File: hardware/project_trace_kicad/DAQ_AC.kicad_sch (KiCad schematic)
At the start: 55 parts, among them U301 THS4131IDR, U302 MCP6499T, U303 ADS1602, U304 LM4040DBZ-4.1

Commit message: Work on Layout
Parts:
- C303, C304: now not fitted
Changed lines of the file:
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@@
 		(on_board yes)
 		(in_pos_files yes)
-		(dnp no)
+		(dnp yes)
 		(property "Reference" "C303"
 			(at 35.179 136.4572 0)
@@
 		(on_board yes)
 		(in_pos_files yes)
-		(dnp no)
+		(dnp yes)
 		(property "Reference" "C304"
 			(at 47.879 136.4572 0)

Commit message: Rework started
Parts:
- removed C303, C304: 47u, Capacitor_THT:CP_Radial_D6.3mm_P2.50mm, symbol Device:C_Polarized

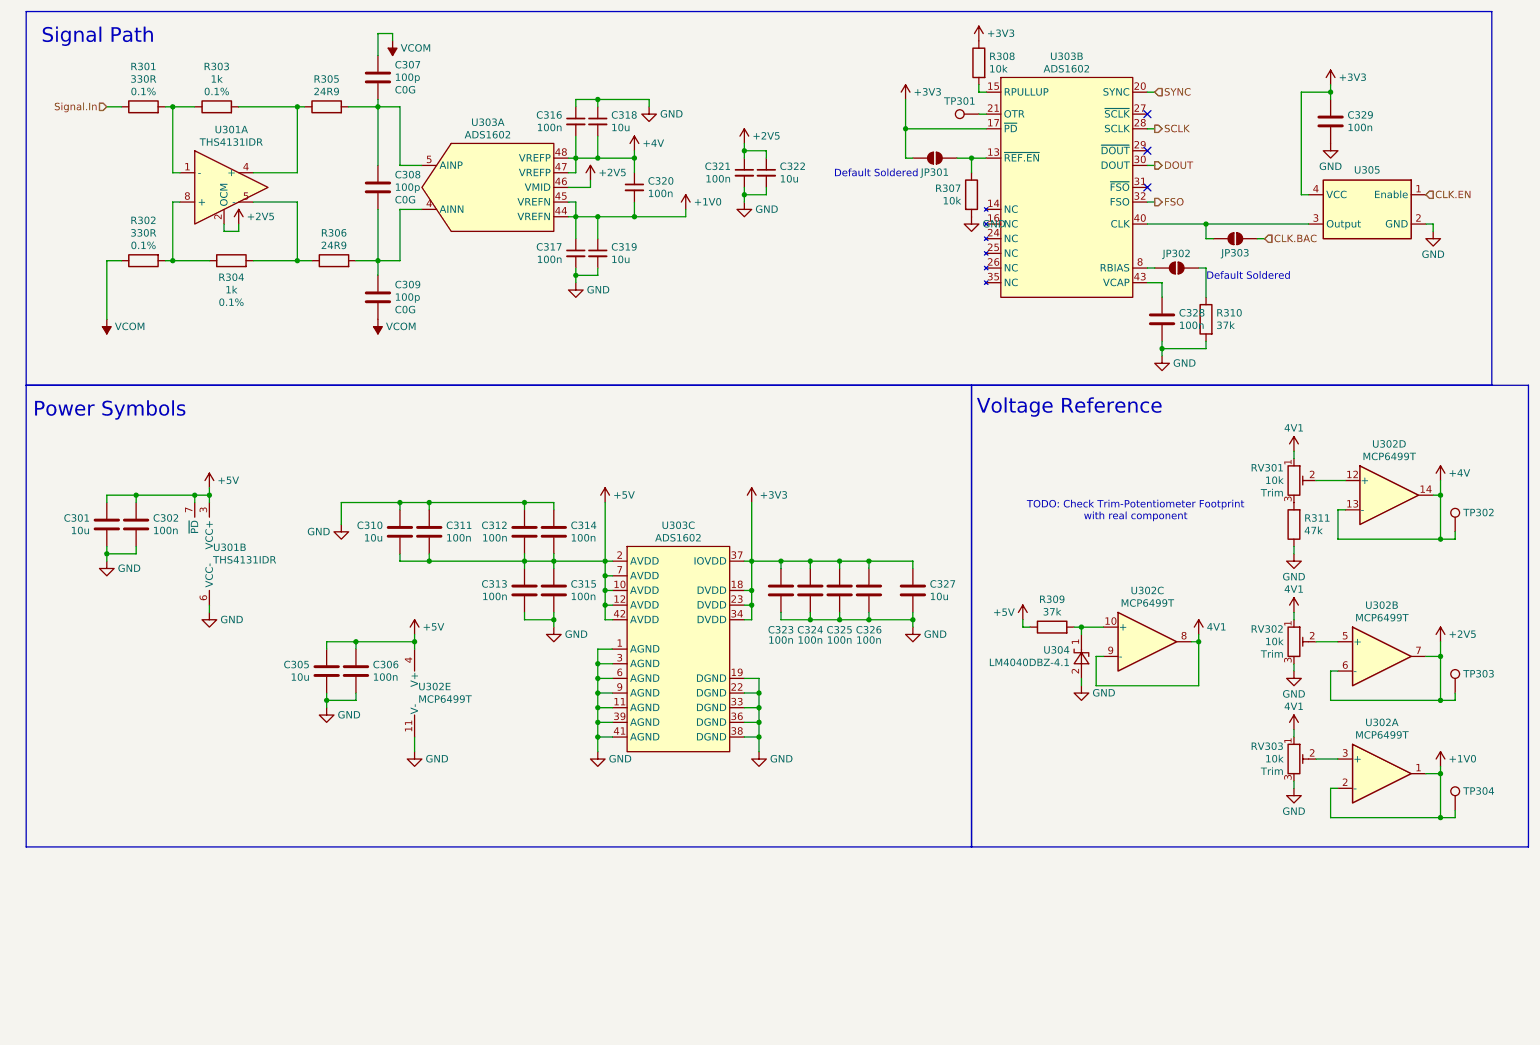
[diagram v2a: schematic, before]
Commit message: Fix inconsistency with ADC datasheet, fix DRC Errors
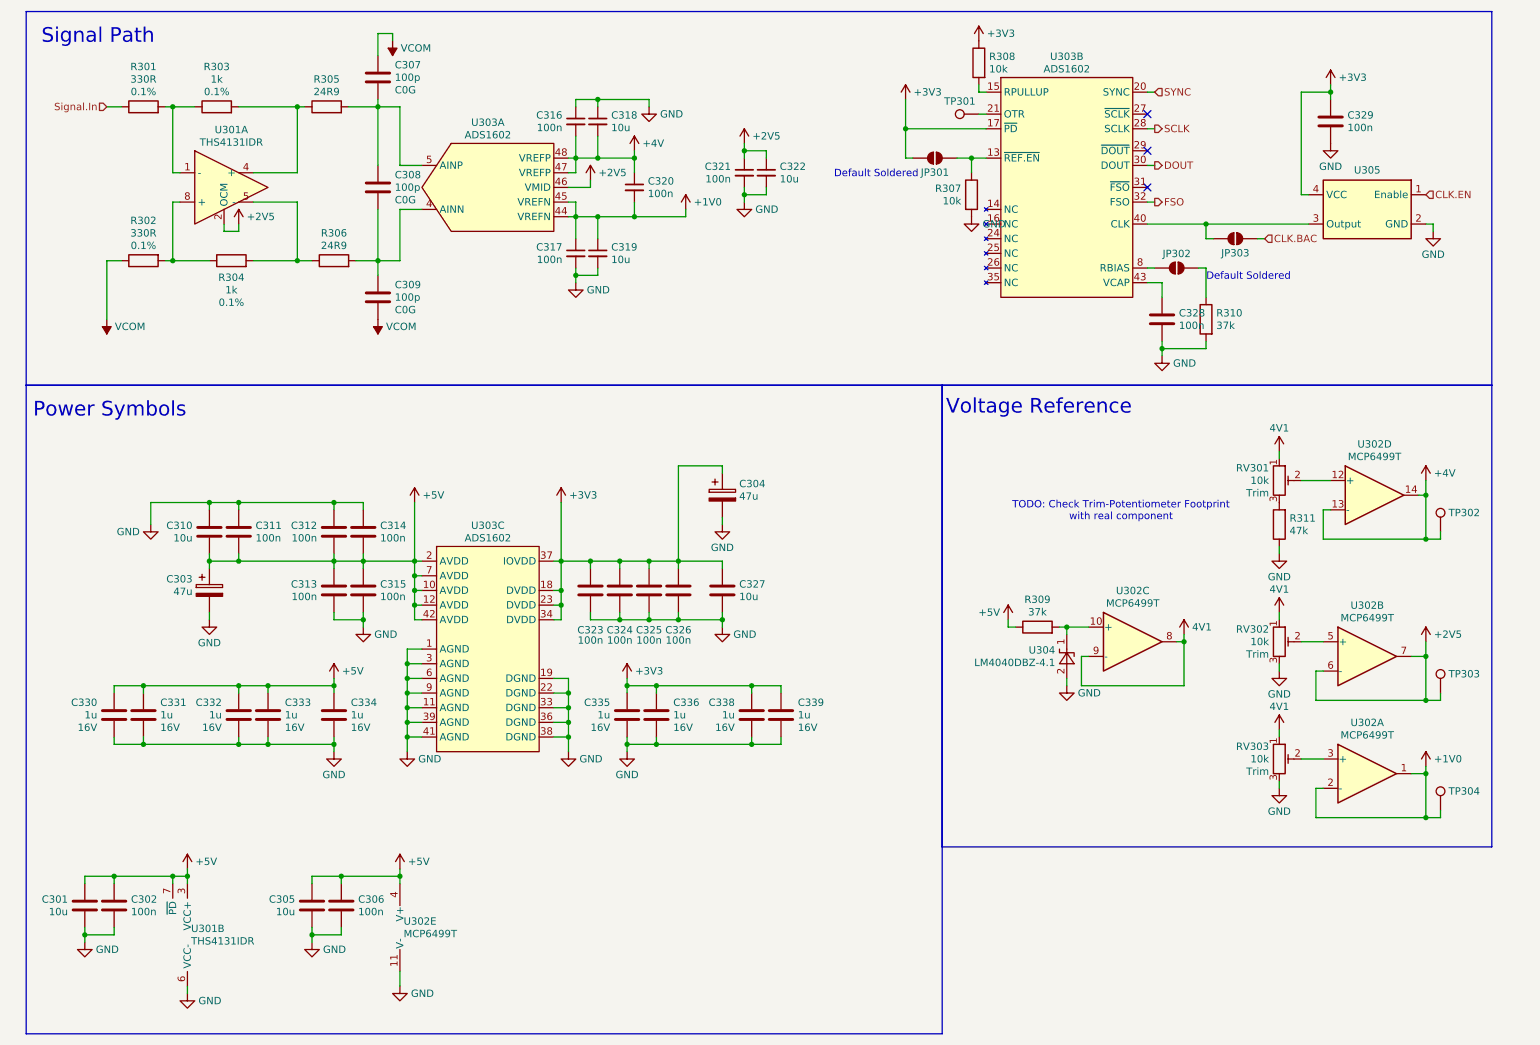
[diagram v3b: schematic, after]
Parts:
- added C303, C304: 47u, Capacitor_THT:CP_Radial_D6.3mm_P2.50mm, symbol Device:C_Polarized
- added C330, C331, C332, C333, C334, C335, C336, C338, C339: 1u, Capacitor_SMD:C_0603_1608Metric_Pad1.08x0.95mm_HandSolder, symbol Device:C
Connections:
- net +3V3: now also C304.1, C335.2, C336.2, C338.2, C339.2
- net +5V: now also C303.1, C330.2, C331.2, C332.2, C333.2, C334.2
- net GND: now also C303.2, C304.2, C330.1, C331.1, C332.1, C333.1, C334.1, C335.1, C336.1, C338.1, C339.1
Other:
- moved on the sheet: C301, C302, C305, C306, C310, C311, C312, C313, C314, C315, C323, C324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

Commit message: Improvements to Power layout and Silkscreen
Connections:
- net ADC.CLK_IN: now reaches JP303.2 (B), U303.40 (CLK), U305.3 (Output)

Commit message: Pre Diffamp
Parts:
- added C337: 100n, Capacitor_SMD:C_0603_1608Metric_Pad1.08x0.95mm_HandSolder, symbol Device:C_Small
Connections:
- net +2V5: now also C337.1
- net GND: now also C337.2

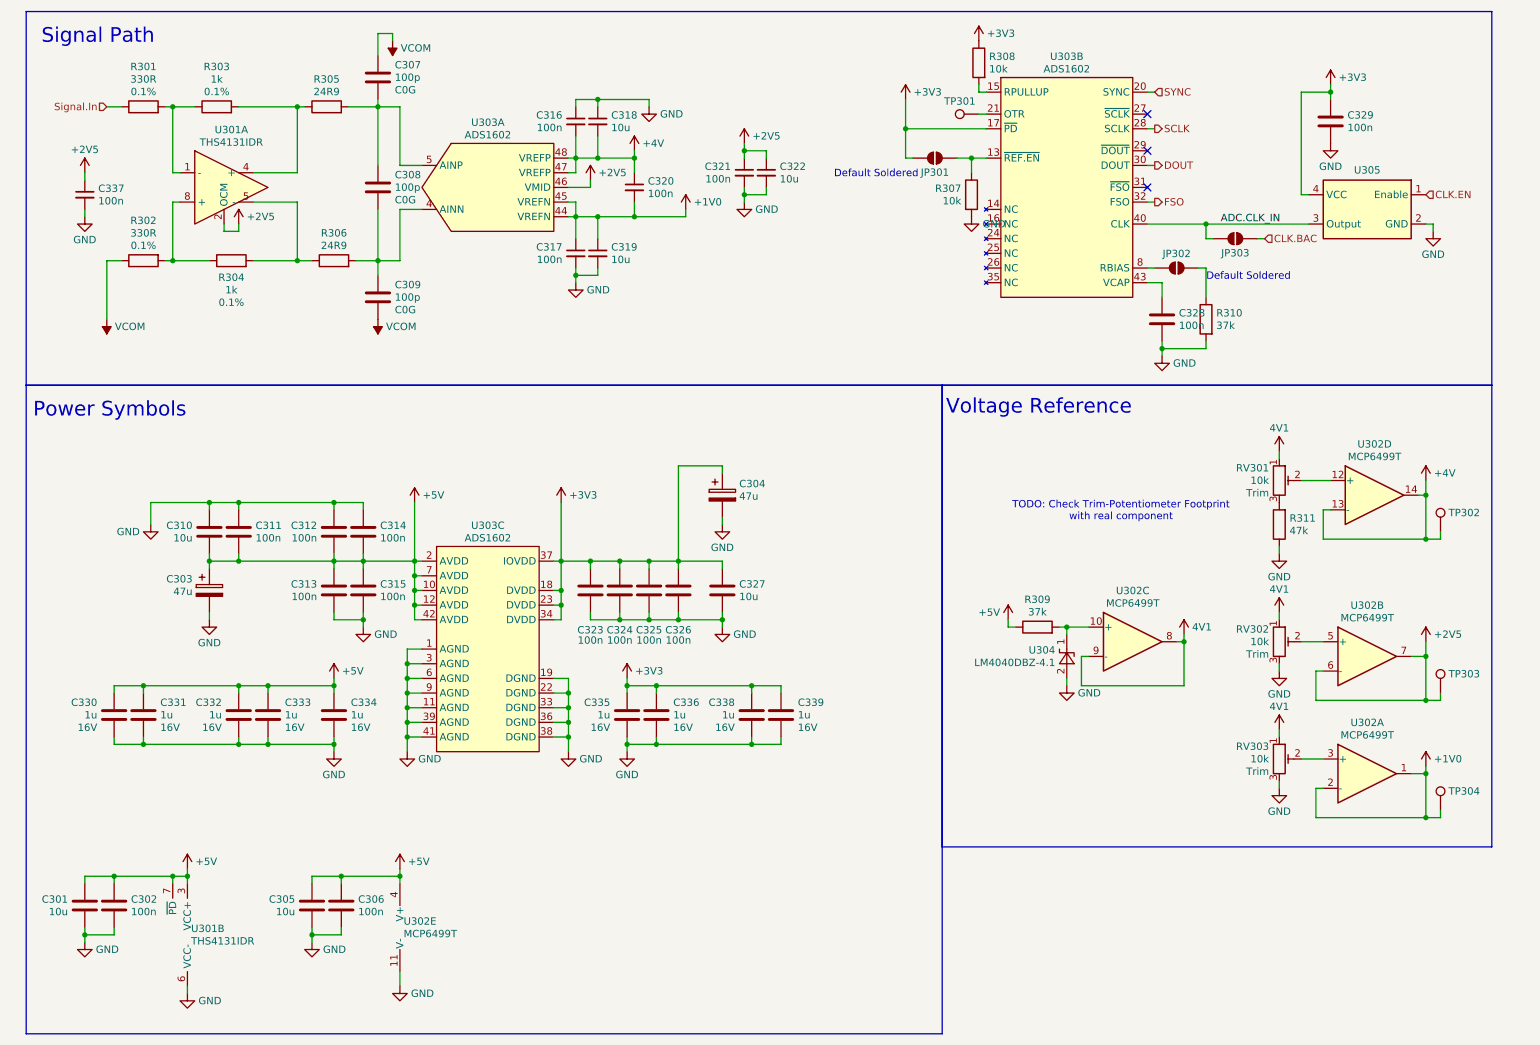
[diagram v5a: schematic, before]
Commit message: Implement new DiffAmp, Small Improvements
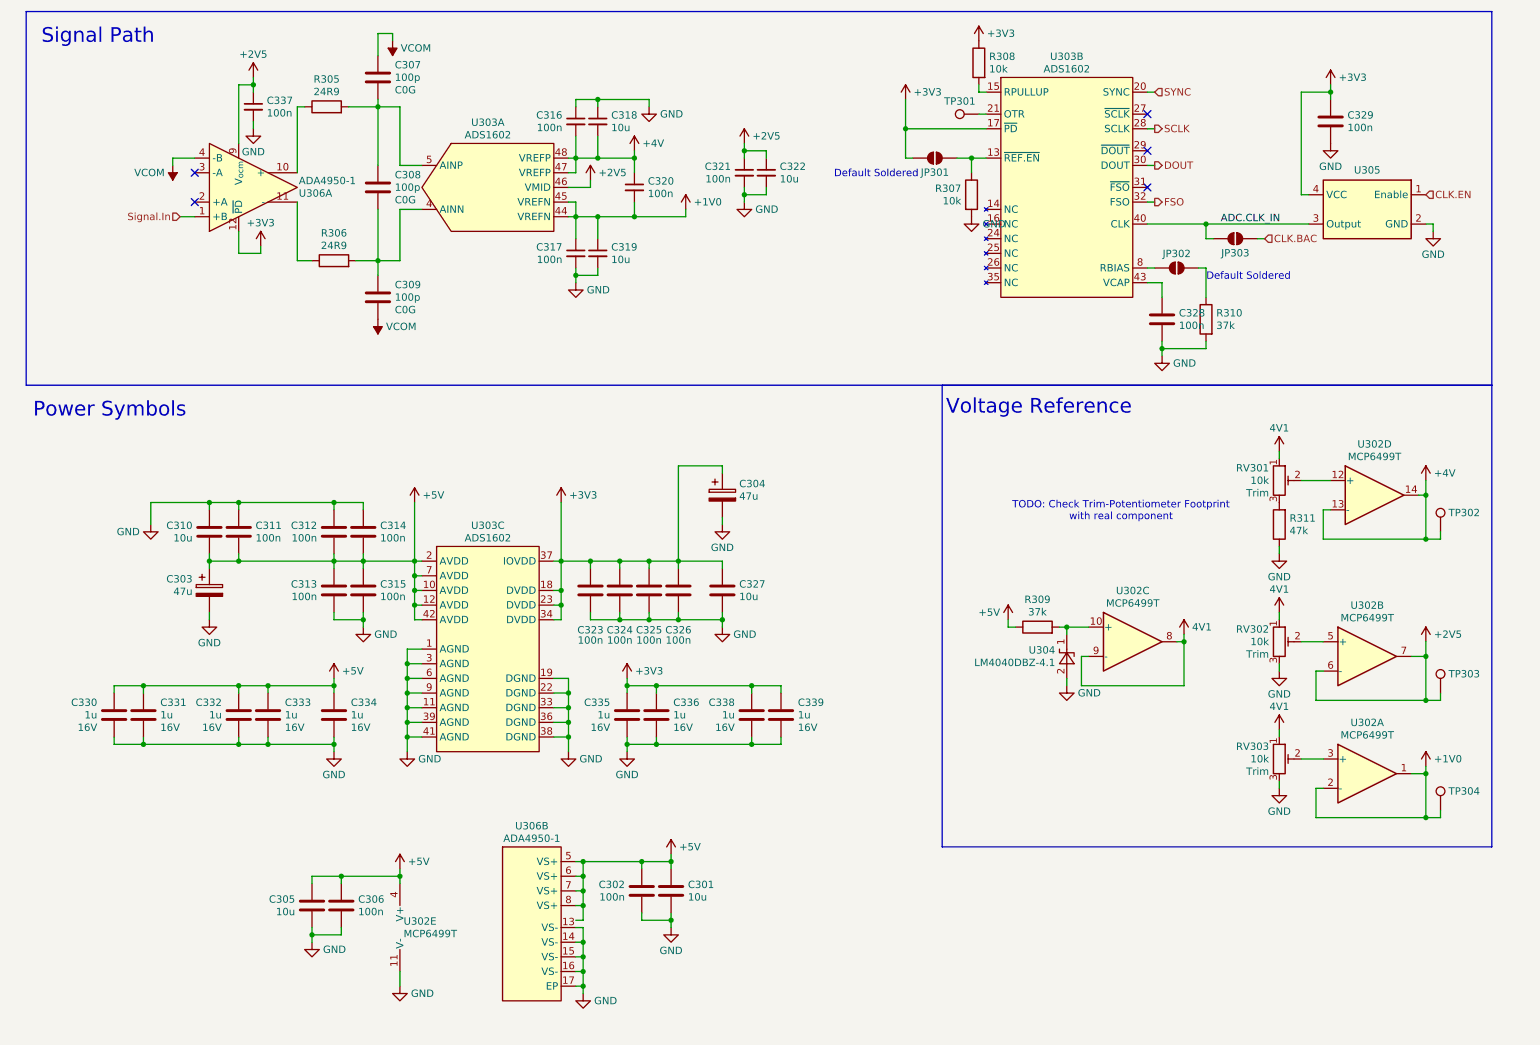
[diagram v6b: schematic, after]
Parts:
- removed R301, R302: 330R, Resistor_SMD:R_0603_1608Metric_Pad0.98x0.95mm_HandSolder, symbol Device:R
- removed R303, R304: 1k, Resistor_SMD:R_0603_1608Metric_Pad0.98x0.95mm_HandSolder, symbol Device:R
- removed U301: THS4131IDR, ProjectTraceFootprints:SOIC8 - D0008A - THS4131IDR, symbol ProjectTraceSymbols:THS4131IDR
- added U306: ADA4950-1, ProjectTraceFootprints:ADA4950-QFN-16_EP_3.1x3.1_Pitch0.5mm, symbol ProjectTraceSymbols:ADA4950-1
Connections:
- net +2V5: now also U306.9 (V_{ocm})
- net +3V3: now also U306.12 (~{PD})
- net +5V: now also U306.5 (VS+), U306.6 (VS+), U306.7 (VS+), U306.8 (VS+)
- net GND: now also U306.13 (VS-), U306.14 (VS-), U306.15 (VS-), U306.16 (VS-), U306.17 (EP)
- net Signal.In: now also U306.1 (+B)
- net VCOM: now also U306.4 (-B)
- net at R306.1: now also U306.11 (-)
- net at R305.1: now also U306.10 (+)
- no-connect marks 3 -> 5
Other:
- moved on the sheet: C301, C302, C337
